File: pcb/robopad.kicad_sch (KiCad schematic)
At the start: 34 parts, among them IC1 Left Slider, IC2 Right Slider, SW1 SW_Push, SW2 SW_Push, SW3 SW_Push, SW4 SW_Push, SW5 SW_Push, SW6 SW_Push, SW7 SW_Push, SW8 SW_Push, SW9 SW_Push, U1 XIAO-RP2040-DIP, U2 Left Joystick, U3 Right Joystick, U4 MCP23008-xP, U5 MCP3426Axx-xSN

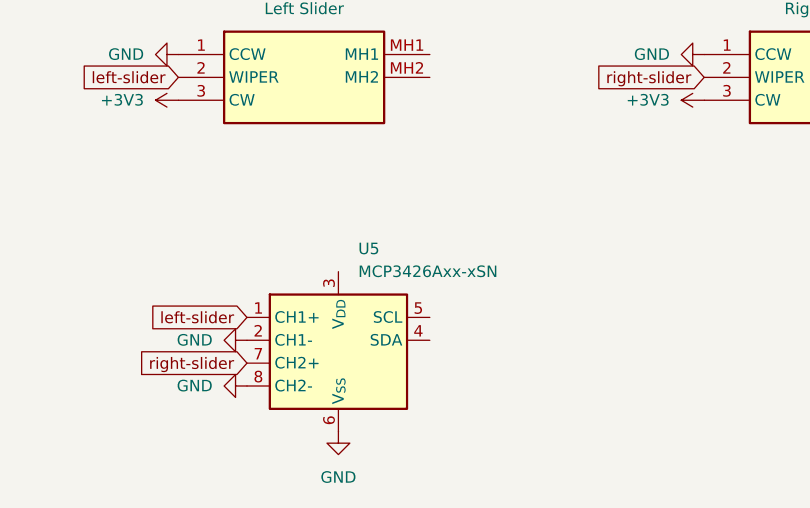
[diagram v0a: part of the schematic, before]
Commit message: Plug in sda/scl
Signed-off-by: Urjith Mishra <66270347+TheScientist101@users.noreply.github.com>
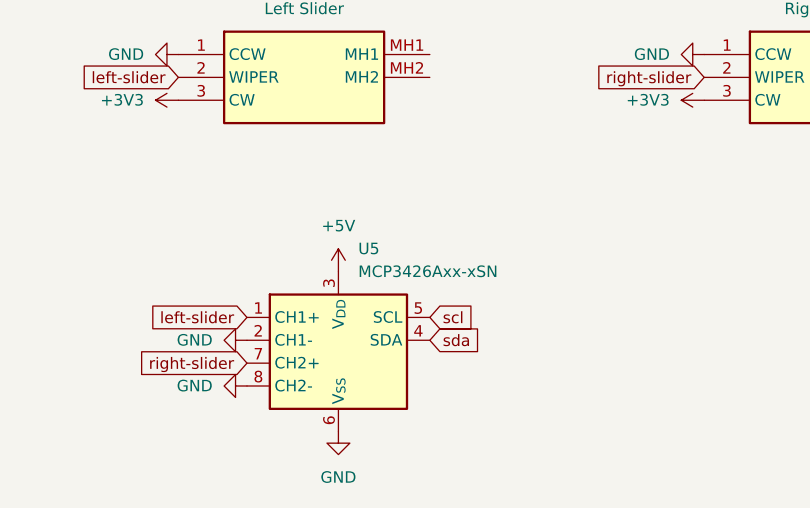
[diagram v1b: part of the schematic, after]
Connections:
- net +5V: now also U5.3 (V_{DD})
- net scl: now also U5.5 (SCL)
- net sda: now also U5.4 (SDA)
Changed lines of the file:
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@@
 		)
 	)
+	(global_label "scl"
+		(shape input)
+		(at 72.39 156.21 0)
+		(fields_autoplaced yes)
+		(effects
+			(font
+				(size 1.27 1.27)
+			)
+			(justify left)
+		)
+		(property "Intersheetrefs" "${INTERSHEET_REFS}"
+			(at 78.1571 156.21 0)
+			(effects
+				(font
+					(size 1.27 1.27)
+				)
+				(justify left)
+				(hide yes)
+			)
+		)
+	)
 	(global_label "row 3"
 		(shape input)
@@
 		)
 	)
+	(global_label "sda"
+		(shape input)
+		(at 72.39 158.75 0)
+		(fields_autoplaced yes)
+		(effects
+			(font
+				(size 1.27 1.27)
+			)
+			(justify left)
+		)
+		(property "Intersheetrefs" "${INTERSHEET_REFS}"
+			(at 78.7013 158.75 0)
+			(effects
+				(font
+					(size 1.27 1.27)
+				)
+				(justify left)
+				(hide yes)
+			)
+		)
+	)
 	(global_label "right-slider"
 		(shape input)
@@
 					(unit 1)
 				)
+			)
+		)
+	)
+	(symbol
+		(lib_id "power:+5V")
+		(at 62.23 151.13 0)
+		(unit 1)
+		(exclude_from_sim no)
+		(in_bom yes)
+		(on_board yes)
+		(dnp no)
+		(fields_autoplaced yes)
+		(property "Reference" "#PWR031"
+			(at 62.23 154.94 0)
+			(effects
+				(font
+					(size 1.27 1.27)
+				)
+				(hide yes)
+			)
+		)
+		(property "Value" "+5V"
+			(at 62.23 146.05 0)
+			(effects
+				(font
+					(size 1.27 1.27)
+				)
+			)
+		)
+		(property "Footprint" ""
+			(at 62.23 151.13 0)
+			(effects
+				(font
+					(size 1.27 1.27)
+				)
+				(hide yes)
+			)
+		)
+		(property "Datasheet" ""
+			(at 62.23 151.13 0)
+			(effects
+				(font
+					(size 1.27 1.27)
+				)
+				(hide yes)
+			)
+		)
+		(property "Description" "Power symbol creates a global label with name \"+5V\""
+			(at 62.23 151.13 0)
+			(effects
+				(font
+					(size 1.27 1.27)
+				)
+				(hide yes)
+			)
+		)
+		(pin "1"
+		)
+		(instances
+			(project "robopad"
+				(path "/cfb0e649-3652-4627-a470-22ef61c07fac"
+					(reference "#PWR031")
+					(unit 1)
+				)
